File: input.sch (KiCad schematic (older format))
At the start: 13 parts

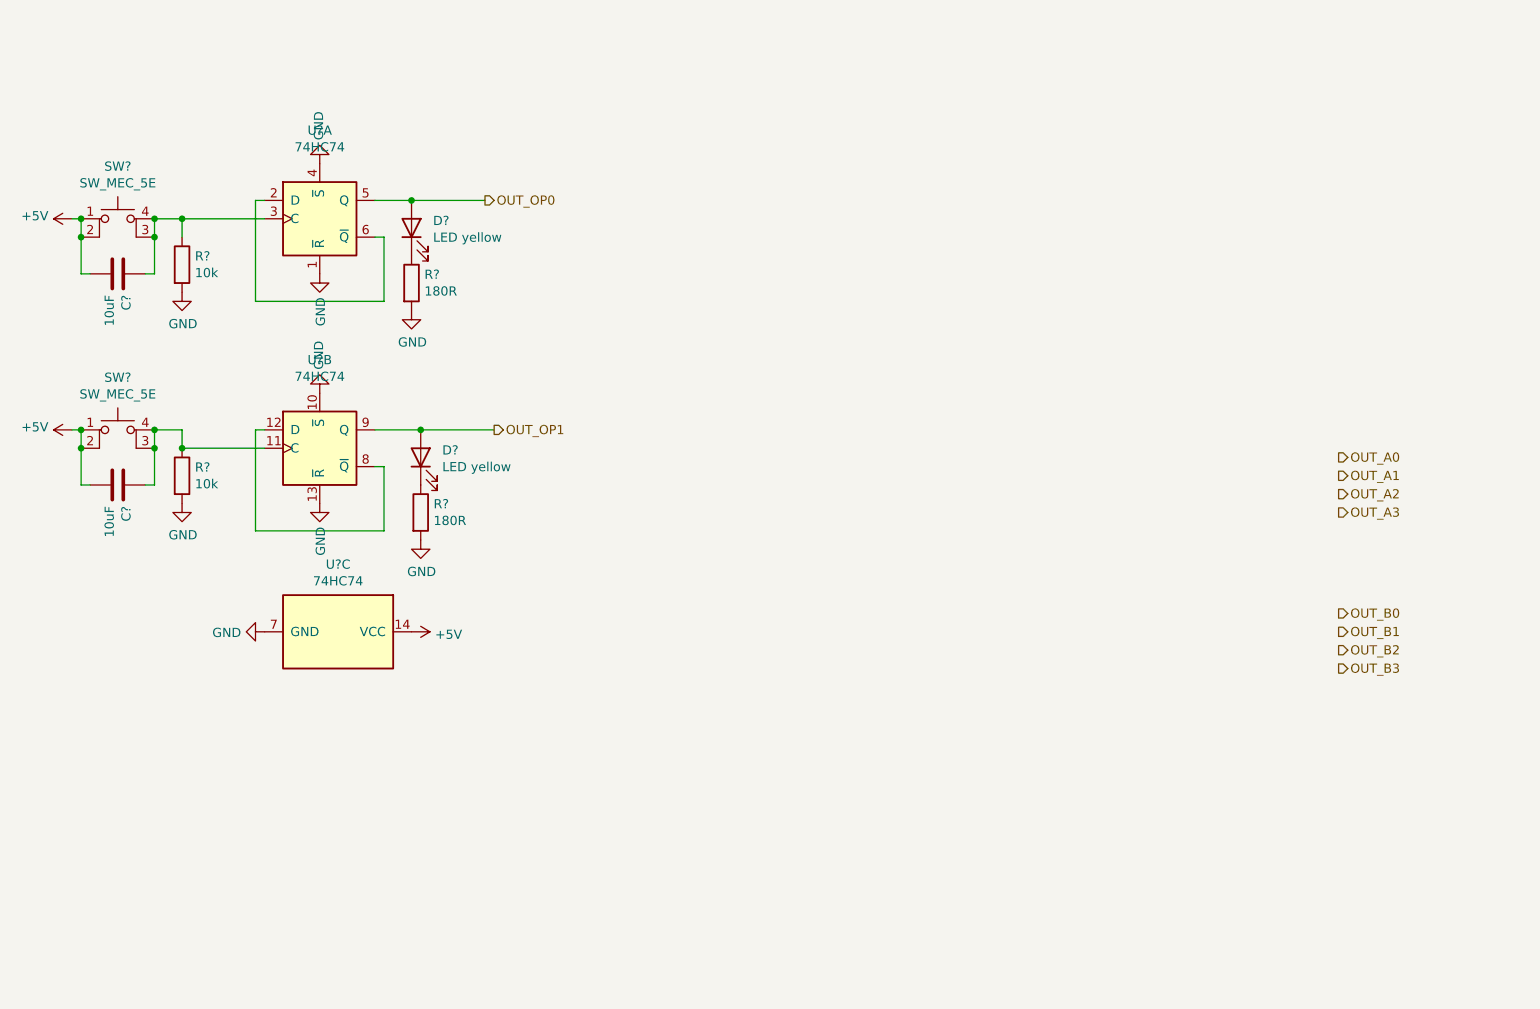
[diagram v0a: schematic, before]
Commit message: Add input switches
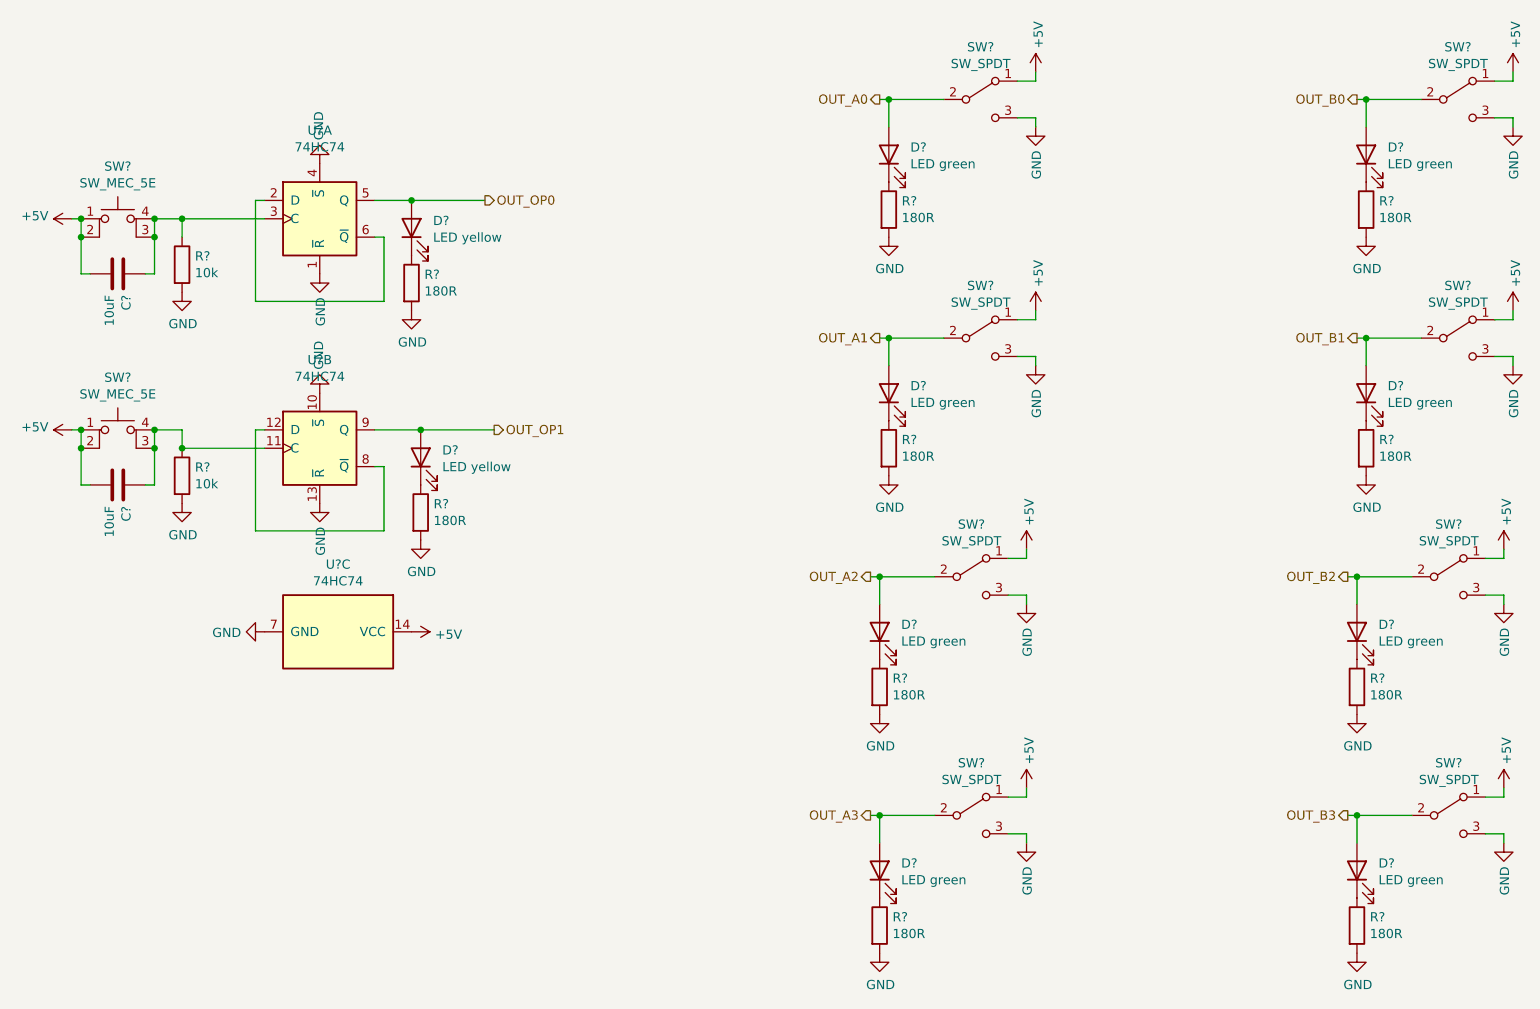
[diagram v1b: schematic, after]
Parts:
- added D? (x8): LED green, LEDs:LED_0603, symbol Device:LED
- added R? (x8): 180R, Resistors_SMD:R_0603, symbol Device:R
- added SW? (x8): SW_SPDT, PB170:toggleSwitch, symbol Switch:SW_SPDT
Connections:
- net +5V: now also SW?.1 (A), SW?.1 (A), SW?.1 (A), SW?.1 (A), SW?.1 (A), SW?.1 (A), SW?.1 (A), SW?.1 (A)
- net GND: now also R?.2, R?.2, R?.2, R?.2, R?.2, R?.2, R?.2, R?.2, SW?.3 (C), SW?.3 (C), SW?.3 (C), SW?.3 (C), SW?.3 (C), SW?.3 (C), SW?.3 (C), SW?.3 (C)
- net OUT_A0: now also D?.2 (A), SW?.2 (B)
- net OUT_A1: now also D?.2 (A), SW?.2 (B)
- net OUT_A2: now also D?.2 (A), SW?.2 (B)
- net OUT_A3: now also D?.2 (A), SW?.2 (B)
- net OUT_B0: now also D?.2 (A), SW?.2 (B)
- net OUT_B1: now also D?.2 (A), SW?.2 (B)
- net OUT_B2: now also D?.2 (A), SW?.2 (B)
- net OUT_B3: now also D?.2 (A), SW?.2 (B)
- new net: D?.1 (K), R?.1 (x8)

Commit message: Annotate components in input and output
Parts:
- gave numbers to parts that had none: 34

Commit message: tiny fixes in annotation
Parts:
- gave numbers to parts that had none: 1
- renumbered C1 to C3, C2 to C4

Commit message: Change R, C and LED footprints
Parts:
- C3, C4: footprint Capacitors_SMD:C_0805 -> Capacitor_SMD:C_0805_2012Metric
- D10, D11, D12, D13, D14, D15, D16, D17, D8, D9: footprint LEDs:LED_0603 -> LED_SMD:LED_0603_1608Metric
- R10, R11, R12, R13, R14, R15, R16, R17, R18, R19, R8, R9: footprint Resistors_SMD:R_0603 -> Resistor_SMD:R_0603_1608Metric
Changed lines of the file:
@@
 F 0 "R10" H 1670 3096 50  0000 L CNN
 F 1 "10k" H 1670 3005 50  0000 L CNN
-F 2 "Resistors_SMD:R_0603" V 1530 3050 50  0001 C CNN
+F 2 "Resistor_SMD:R_0603_1608Metric" V 1530 3050 50  0001 C CNN
 F 3 "https://datasheet.lcsc.com/szlcsc/Uniroyal-Elec-0603WAF1002T5E_C25804.pdf" H 1600 3050 50  0001 C CNN
 F 4 "C25804" H 1600 3050 50  0001 C CNN "LCSC"
@@
 F 0 "C4" H 1365 3146 50  0000 L CNN
 F 1 "10uF" H 1365 3055 50  0000 L CNN
-F 2 "Capacitors_SMD:C_0805" H 1288 2950 50  0001 C CNN
+F 2 "Capacitor_SMD:C_0805_2012Metric" H 1288 2950 50  0001 C CNN
 F 3 "https://datasheet.lcsc.com/szlcsc/Samsung-Electro-Mechanics-CL21A106KAYNNNE_C15850.pdf" H 1250 3100 50  0001 C CNN
 F 4 "C15850" H 1250 3100 50  0001 C CNN "LCSC"
@@
 F 0 "R11" H 2970 3296 50  0000 L CNN
 F 1 "180R" H 2970 3205 50  0000 L CNN
-F 2 "Resistors_SMD:R_0603" V 2830 3250 50  0001 C CNN
+F 2 "Resistor_SMD:R_0603_1608Metric" V 2830 3250 50  0001 C CNN
 F 3 "https://datasheet.lcsc.com/szlcsc/Uniroyal-Elec-0603WAF1800T5E_C22828.pdf" H 2900 3250 50  0001 C CNN
 F 4 "C22828" H 2900 3250 50  0001 C CNN "LCSC"
@@
 F 0 "R8" H 1670 1946 50  0000 L CNN
 F 1 "10k" H 1670 1855 50  0000 L CNN
-F 2 "Resistors_SMD:R_0603" V 1530 1900 50  0001 C CNN
+F 2 "Resistor_SMD:R_0603_1608Metric" V 1530 1900 50  0001 C CNN
 F 3 "https://datasheet.lcsc.com/szlcsc/Uniroyal-Elec-0603WAF1002T5E_C25804.pdf" H 1600 1900 50  0001 C CNN
 F 4 "C25804" H 1600 1900 50  0001 C CNN "LCSC"
@@
 F 0 "C3" H 1365 1996 50  0000 L CNN
 F 1 "10uF" H 1365 1905 50  0000 L CNN
-F 2 "Capacitors_SMD:C_0805" H 1288 1800 50  0001 C CNN
+F 2 "Capacitor_SMD:C_0805_2012Metric" H 1288 1800 50  0001 C CNN
 F 3 "https://datasheet.lcsc.com/szlcsc/Samsung-Electro-Mechanics-CL21A106KAYNNNE_C15850.pdf" H 1250 1950 50  0001 C CNN
 F 4 "C15850" H 1250 1950 50  0001 C CNN "LCSC"
@@
 F 0 "R9" H 2920 2046 50  0000 L CNN
 F 1 "180R" H 2920 1955 50  0000 L CNN
-F 2 "Resistors_SMD:R_0603" V 2780 2000 50  0001 C CNN
+F 2 "Resistor_SMD:R_0603_1608Metric" V 2780 2000 50  0001 C CNN
 F 3 "https://datasheet.lcsc.com/szlcsc/Uniroyal-Elec-0603WAF1800T5E_C22828.pdf" H 2850 2000 50  0001 C CNN
 F 4 "C22828" H 2850 2000 50  0001 C CNN "LCSC"
@@
 F 0 "D8" V 2889 1583 50  0000 R CNN
 F 1 "LED yellow" V 2798 1583 50  0000 R CNN
-F 2 "LEDs:LED_0603" H 2850 1700 50  0001 C CNN
+F 2 "LED_SMD:LED_0603_1608Metric" H 2850 1700 50  0001 C CNN
 F 3 "https://datasheet.lcsc.com/szlcsc/1810101813_Everlight-Elec-19-213-Y2C-CQ2R2L-3T-CY_C72038.pdf" H 2850 1700 50  0001 C CNN
 F 4 "C72038" V 2850 1700 50  0001 C CNN "LCSC"
@@
 F 0 "D9" V 2939 2833 50  0000 R CNN
 F 1 "LED yellow" V 2848 2833 50  0000 R CNN
-F 2 "LEDs:LED_0603" H 2900 2950 50  0001 C CNN
+F 2 "LED_SMD:LED_0603_1608Metric" H 2900 2950 50  0001 C CNN
 F 3 "https://datasheet.lcsc.com/szlcsc/1810101813_Everlight-Elec-19-213-Y2C-CQ2R2L-3T-CY_C72038.pdf" H 2900 2950 50  0001 C CNN
 F 4 "C72038" V 2900 2950 50  0001 C CNN "LCSC"
@@
 F 0 "R12" H 5520 1646 50  0000 L CNN
 F 1 "180R" H 5520 1555 50  0000 L CNN
-F 2 "Resistors_SMD:R_0603" V 5380 1600 50  0001 C CNN
+F 2 "Resistor_SMD:R_0603_1608Metric" V 5380 1600 50  0001 C CNN
 F 3 "https://datasheet.lcsc.com/szlcsc/Uniroyal-Elec-0603WAF1800T5E_C22828.pdf" H 5450 1600 50  0001 C CNN
 F 4 "C22828" H 5450 1600 50  0001 C CNN "LCSC"
@@
 F 0 "D10" V 5489 1183 50  0000 R CNN
 F 1 "LED green" V 5398 1183 50  0000 R CNN
-F 2 "LEDs:LED_0603" H 5450 1300 50  0001 C CNN
+F 2 "LED_SMD:LED_0603_1608Metric" H 5450 1300 50  0001 C CNN
 F 3 "https://datasheet.lcsc.com/szlcsc/1811101510_Everlight-Elec-19-217-GHC-YR1S2-3T_C72043.pdf" H 5450 1300 50  0001 C CNN
 F 4 "C72043" V 5450 1300 50  0001 C CNN "LCSC"
@@
 F 0 "R19" H 5520 2946 50  0000 L CNN
 F 1 "180R" H 5520 2855 50  0000 L CNN
-F 2 "Resistors_SMD:R_0603" V 5380 2900 50  0001 C CNN
+F 2 "Resistor_SMD:R_0603_1608Metric" V 5380 2900 50  0001 C CNN
 F 3 "https://datasheet.lcsc.com/szlcsc/Uniroyal-Elec-0603WAF1800T5E_C22828.pdf" H 5450 2900 50  0001 C CNN
 F 4 "C22828" H 5450 2900 50  0001 C CNN "LCSC"
@@
 F 0 "D11" V 5489 2483 50  0000 R CNN
 F 1 "LED green" V 5398 2483 50  0000 R CNN
-F 2 "LEDs:LED_0603" H 5450 2600 50  0001 C CNN
+F 2 "LED_SMD:LED_0603_1608Metric" H 5450 2600 50  0001 C CNN
 F 3 "https://datasheet.lcsc.com/szlcsc/1811101510_Everlight-Elec-19-217-GHC-YR1S2-3T_C72043.pdf" H 5450 2600 50  0001 C CNN
 F 4 "C72043" V 5450 2600 50  0001 C CNN "LCSC"
@@
 F 0 "R13" H 5470 4246 50  0000 L CNN
 F 1 "180R" H 5470 4155 50  0000 L CNN
-F 2 "Resistors_SMD:R_0603" V 5330 4200 50  0001 C CNN
+F 2 "Resistor_SMD:R_0603_1608Metric" V 5330 4200 50  0001 C CNN
 F 3 "https://datasheet.lcsc.com/szlcsc/Uniroyal-Elec-0603WAF1800T5E_C22828.pdf" H 5400 4200 50  0001 C CNN
 F 4 "C22828" H 5400 4200 50  0001 C CNN "LCSC"
@@
 F 0 "D12" V 5439 3783 50  0000 R CNN
 F 1 "LED green" V 5348 3783 50  0000 R CNN
-F 2 "LEDs:LED_0603" H 5400 3900 50  0001 C CNN
+F 2 "LED_SMD:LED_0603_1608Metric" H 5400 3900 50  0001 C CNN
 F 3 "https://datasheet.lcsc.com/szlcsc/1811101510_Everlight-Elec-19-217-GHC-YR1S2-3T_C72043.pdf" H 5400 3900 50  0001 C CNN
 F 4 "C72043" V 5400 3900 50  0001 C CNN "LCSC"
@@
 F 0 "R14" H 5470 5546 50  0000 L CNN
 F 1 "180R" H 5470 5455 50  0000 L CNN
-F 2 "Resistors_SMD:R_0603" V 5330 5500 50  0001 C CNN
+F 2 "Resistor_SMD:R_0603_1608Metric" V 5330 5500 50  0001 C CNN
 F 3 "https://datasheet.lcsc.com/szlcsc/Uniroyal-Elec-0603WAF1800T5E_C22828.pdf" H 5400 5500 50  0001 C CNN
 F 4 "C22828" H 5400 5500 50  0001 C CNN "LCSC"
@@
 F 0 "D13" V 5439 5083 50  0000 R CNN
 F 1 "LED green" V 5348 5083 50  0000 R CNN
-F 2 "LEDs:LED_0603" H 5400 5200 50  0001 C CNN
+F 2 "LED_SMD:LED_0603_1608Metric" H 5400 5200 50  0001 C CNN
 F 3 "https://datasheet.lcsc.com/szlcsc/1811101510_Everlight-Elec-19-217-GHC-YR1S2-3T_C72043.pdf" H 5400 5200 50  0001 C CNN
 F 4 "C72043" V 5400 5200 50  0001 C CNN "LCSC"
@@
 F 0 "R15" H 8120 1646 50  0000 L CNN
 F 1 "180R" H 8120 1555 50  0000 L CNN
-F 2 "Resistors_SMD:R_0603" V 7980 1600 50  0001 C CNN
+F 2 "Resistor_SMD:R_0603_1608Metric" V 7980 1600 50  0001 C CNN
 F 3 "https://datasheet.lcsc.com/szlcsc/Uniroyal-Elec-0603WAF1800T5E_C22828.pdf" H 8050 1600 50  0001 C CNN
 F 4 "C22828" H 8050 1600 50  0001 C CNN "LCSC"
@@
 F 0 "D14" V 8089 1183 50  0000 R CNN
 F 1 "LED green" V 7998 1183 50  0000 R CNN
-F 2 "LEDs:LED_0603" H 8050 1300 50  0001 C CNN
+F 2 "LED_SMD:LED_0603_1608Metric" H 8050 1300 50  0001 C CNN
 F 3 "https://datasheet.lcsc.com/szlcsc/1811101510_Everlight-Elec-19-217-GHC-YR1S2-3T_C72043.pdf" H 8050 1300 50  0001 C CNN
 F 4 "C72043" V 8050 1300 50  0001 C CNN "LCSC"
@@
 F 0 "R16" H 8120 2946 50  0000 L CNN
 F 1 "180R" H 8120 2855 50  0000 L CNN
-F 2 "Resistors_SMD:R_0603" V 7980 2900 50  0001 C CNN
+F 2 "Resistor_SMD:R_0603_1608Metric" V 7980 2900 50  0001 C CNN
 F 3 "https://datasheet.lcsc.com/szlcsc/Uniroyal-Elec-0603WAF1800T5E_C22828.pdf" H 8050 2900 50  0001 C CNN
 F 4 "C22828" H 8050 2900 50  0001 C CNN "LCSC"
@@
 F 0 "D15" V 8089 2483 50  0000 R CNN
 F 1 "LED green" V 7998 2483 50  0000 R CNN
-F 2 "LEDs:LED_0603" H 8050 2600 50  0001 C CNN
+F 2 "LED_SMD:LED_0603_1608Metric" H 8050 2600 50  0001 C CNN
 F 3 "https://datasheet.lcsc.com/szlcsc/1811101510_Everlight-Elec-19-217-GHC-YR1S2-3T_C72043.pdf" H 8050 2600 50  0001 C CNN
 F 4 "C72043" V 8050 2600 50  0001 C CNN "LCSC"
@@
 F 0 "R17" H 8070 4246 50  0000 L CNN
 F 1 "180R" H 8070 4155 50  0000 L CNN
-F 2 "Resistors_SMD:R_0603" V 7930 4200 50  0001 C CNN
+F 2 "Resistor_SMD:R_0603_1608Metric" V 7930 4200 50  0001 C CNN
 F 3 "https://datasheet.lcsc.com/szlcsc/Uniroyal-Elec-0603WAF1800T5E_C22828.pdf" H 8000 4200 50  0001 C CNN
 F 4 "C22828" H 8000 4200 50  0001 C CNN "LCSC"
@@
 F 0 "D16" V 8039 3783 50  0000 R CNN
 F 1 "LED green" V 7948 3783 50  0000 R CNN
-F 2 "LEDs:LED_0603" H 8000 3900 50  0001 C CNN
+F 2 "LED_SMD:LED_0603_1608Metric" H 8000 3900 50  0001 C CNN
 F 3 "https://datasheet.lcsc.com/szlcsc/1811101510_Everlight-Elec-19-217-GHC-YR1S2-3T_C72043.pdf" H 8000 3900 50  0001 C CNN
 F 4 "C72043" V 8000 3900 50  0001 C CNN "LCSC"
@@
 F 0 "R18" H 8070 5546 50  0000 L CNN
 F 1 "180R" H 8070 5455 50  0000 L CNN
-F 2 "Resistors_SMD:R_0603" V 7930 5500 50  0001 C CNN
+F 2 "Resistor_SMD:R_0603_1608Metric" V 7930 5500 50  0001 C CNN
 F 3 "https://datasheet.lcsc.com/szlcsc/Uniroyal-Elec-0603WAF1800T5E_C22828.pdf" H 8000 5500 50  0001 C CNN
 F 4 "C22828" H 8000 5500 50  0001 C CNN "LCSC"
@@
 F 0 "D17" V 8039 5083 50  0000 R CNN
 F 1 "LED green" V 7948 5083 50  0000 R CNN
-F 2 "LEDs:LED_0603" H 8000 5200 50  0001 C CNN
+F 2 "LED_SMD:LED_0603_1608Metric" H 8000 5200 50  0001 C CNN
 F 3 "https://datasheet.lcsc.com/szlcsc/1811101510_Everlight-Elec-19-217-GHC-YR1S2-3T_C72043.pdf" H 8000 5200 50  0001 C CNN
 F 4 "C72043" V 8000 5200 50  0001 C CNN "LCSC"
